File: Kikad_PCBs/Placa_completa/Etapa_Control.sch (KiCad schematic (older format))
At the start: 27 parts, among them U1 UC2844N, U2 PC817, U3 TL431

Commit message: modificaciones al pcb
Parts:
- C5: value 15n -> 1.5n
- RV1: value 5k -> 1k
- Rbledder1: value 22k -> 10K
- Rcs1: value 4k2 -> 3K9
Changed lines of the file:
@@
 P 4800 3450
 F 0 "Rcs1" V 4880 3450 39  0000 C CNN
-F 1 "4k2" V 4800 3450 39  0000 C CNN
+F 1 "3K9" V 4800 3450 39  0000 C CNN
 F 2 "Resistors_THT:R_Axial_DIN0207_L6.3mm_D2.5mm_P7.62mm_Horizontal" V 4730 3450 50  0001 C CNN
 F 3 "" H 4800 3450 50  0001 C CNN
@@
 P 6650 2600
 F 0 "Rbledder1" V 6730 2600 39  0000 C CNN
-F 1 "22k" V 6650 2600 39  0000 C CNN
+F 1 "10K" V 6650 2600 39  0000 C CNN
 F 2 "Resistors_THT:R_Axial_DIN0207_L6.3mm_D2.5mm_P7.62mm_Horizontal" V 6580 2600 50  0001 C CNN
 F 3 "" H 6650 2600 50  0001 C CNN
@@
 P 9600 4600
 F 0 "C5" H 9625 4700 50  0000 L CNN
-F 1 "15n" H 9625 4500 39  0000 L CNN
+F 1 "1.5n" H 9625 4500 39  0000 L CNN
 F 2 "Capacitors_THT:C_Disc_D5.0mm_W2.5mm_P2.50mm" H 9638 4450 50  0001 C CNN
 F 3 "" H 9600 4600 50  0001 C CNN
@@
 P 5850 5450
 F 0 "RV1" V 5675 5450 39  0000 C CNN
-F 1 "5k" V 5750 5450 39  0000 C CNN
+F 1 "1k" V 5750 5450 39  0000 C CNN
 F 2 "Potentiometers:Potentiometer_Trimmer_Bourns_3296W" H 5850 5450 50  0001 C CNN
 F 3 "" H 5850 5450 50  0001 C CNN

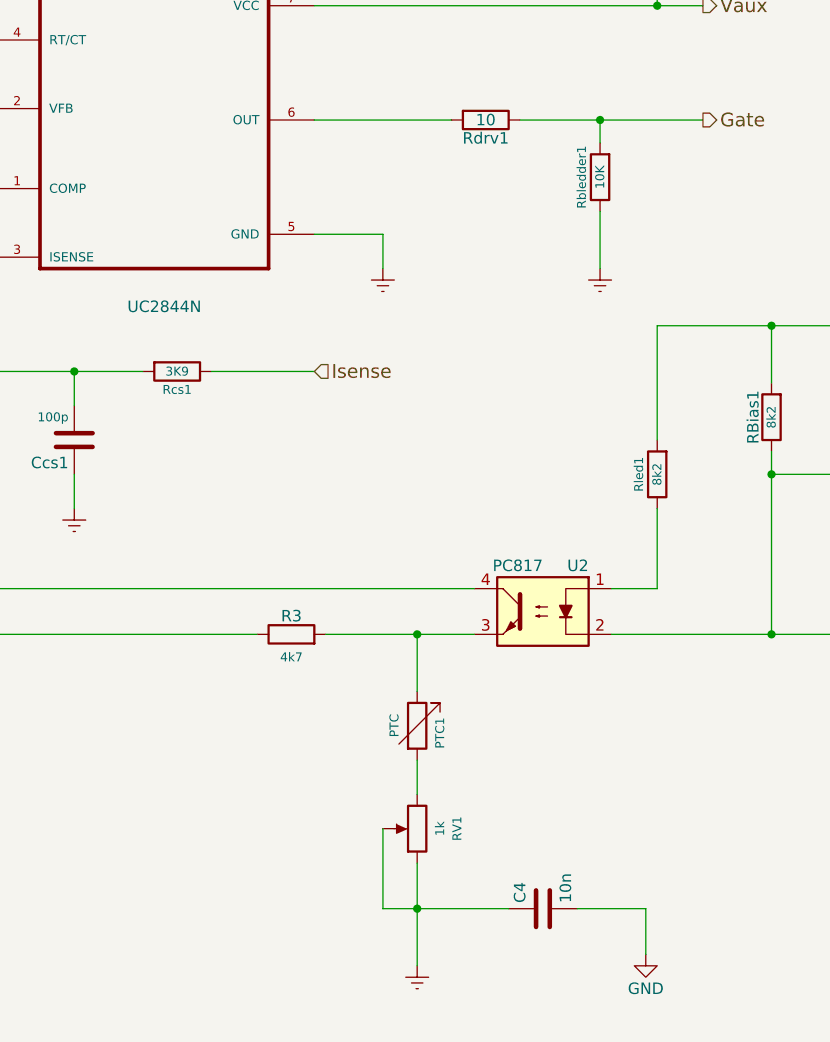
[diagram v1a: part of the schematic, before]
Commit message: cambio proyecto kicad por el que usamos en la primer fuente completa y modificacion de tamaños, bordes rellenos adaptado a la placa final. Falta ver que queden bien las serigrafias y modificar los componentes qe hizo el riojano para que queden todas las serigrafias bien
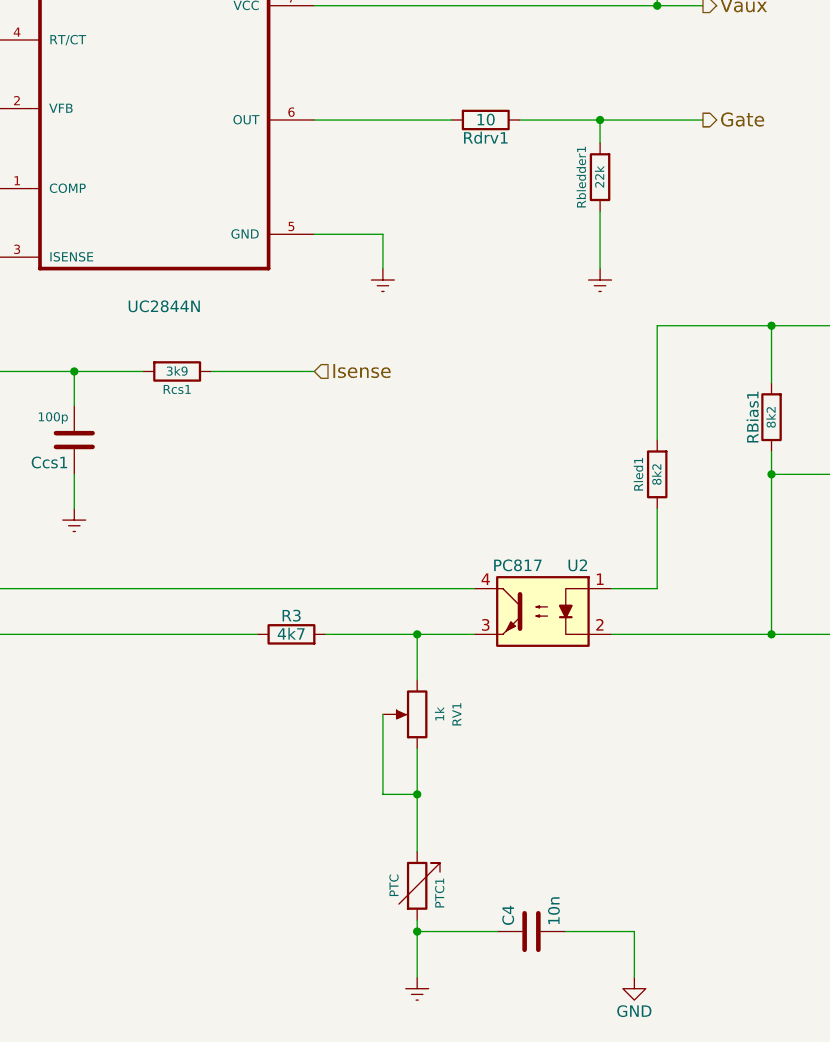
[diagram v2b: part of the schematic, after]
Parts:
- Rbledder1: value 10K -> 22k
- Rcs1: value 3K9 -> 3k9
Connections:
- net Earth: now also PTC1.2; no longer RV1.1, RV1.2
- net at R3.2, U2.3: now also RV1.3; no longer PTC1.1
- new net: PTC1.1, RV1.1, RV1.2
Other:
- moved on the sheet: C4, PTC1, RV1
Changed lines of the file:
@@
 P 4800 3450
 F 0 "Rcs1" V 4880 3450 39  0000 C CNN
-F 1 "3K9" V 4800 3450 39  0000 C CNN
+F 1 "3k9" V 4800 3450 39  0000 C CNN
 F 2 "Resistors_THT:R_Axial_DIN0207_L6.3mm_D2.5mm_P7.62mm_Horizontal" V 4730 3450 50  0001 C CNN
 F 3 "" H 4800 3450 50  0001 C CNN
@@
 P 5300 4600
 F 0 "R3" V 5380 4600 50  0000 C CNN
-F 1 "4k7" V 5200 4600 39  0000 C CNN
+F 1 "4k7" V 5300 4600 50  0000 C CNN
 F 2 "Resistors_THT:R_Axial_DIN0204_L3.6mm_D1.6mm_P7.62mm_Horizontal" V 5230 4600 50  0001 C CNN
 F 3 "" H 5300 4600 50  0001 C CNN
@@
 P 6650 2600
 F 0 "Rbledder1" V 6730 2600 39  0000 C CNN
-F 1 "10K" V 6650 2600 39  0000 C CNN
+F 1 "22k" V 6650 2600 39  0000 C CNN
 F 2 "Resistors_THT:R_Axial_DIN0207_L6.3mm_D2.5mm_P7.62mm_Horizontal" V 6580 2600 50  0001 C CNN
 F 3 "" H 6650 2600 50  0001 C CNN
@@
 L C C4
 U 1 1 5C1827A1
-P 6400 5800
-F 0 "C4" H 6425 5900 50  0000 L CNN
-F 1 "10n" H 6425 5700 50  0000 L CNN
-F 2 "Capacitors_THT:C_Rect_L4.0mm_W2.5mm_P2.50mm" H 6438 5650 50  0001 C CNN
-F 3 "" H 6400 5800 50  0001 C CNN
-	1    6400 5800
+P 6350 5900
+F 0 "C4" H 6375 6000 50  0000 L CNN
+F 1 "10n" H 6375 5800 50  0000 L CNN
+F 2 "Capacitors_THT:C_Rect_L4.0mm_W2.5mm_P2.50mm" H 6388 5750 50  0001 C CNN
+F 3 "" H 6350 5900 50  0001 C CNN
+	1    6350 5900
 	0    -1   -1   0
 $EndComp
@@
 	5450 4600 6100 4600
 Wire Wire Line
+	5850 4600 5850 4800
+Wire Wire Line
 	3300 4600 5150 4600
 Connection ~ 3300 2950
@@
 	8500 6100 8500 5750
 Wire Wire Line
-	6550 5800 6850 5800
-Wire Wire Line
-	5850 5600 5850 6050
+	6500 5900 6800 5900
+Wire Wire Line
+	5850 5100 5850 5550
 $Comp
 L GND #PWR024
 U 1 1 5C182AC4
-P 6850 6000
-F 0 "#PWR024" H 6850 5750 50  0001 C CNN
-F 1 "GND" H 6850 5850 50  0000 C CNN
-F 2 "" H 6850 6000 50  0001 C CNN
-F 3 "" H 6850 6000 50  0001 C CNN
-	1    6850 6000
+P 6800 6100
+F 0 "#PWR024" H 6800 5850 50  0001 C CNN
+F 1 "GND" H 6800 5950 50  0000 C CNN
+F 2 "" H 6800 6100 50  0001 C CNN
+F 3 "" H 6800 6100 50  0001 C CNN
+	1    6800 6100
 	1    0    0    -1
 $EndComp
@@
 L Earth #PWR027
 U 1 1 5C183232
-P 5850 6050
-F 0 "#PWR027" H 5850 5800 50  0001 C CNN
-F 1 "Earth" H 5850 5900 50  0001 C CNN
-F 2 "" H 5850 6050 50  0001 C CNN
-F 3 "" H 5850 6050 50  0001 C CNN
-	1    5850 6050
-	1    0    0    -1
-$EndComp
-Connection ~ 5850 5800
+P 5850 6100
+F 0 "#PWR027" H 5850 5850 50  0001 C CNN
+F 1 "Earth" H 5850 5950 50  0001 C CNN
+F 2 "" H 5850 6100 50  0001 C CNN
+F 3 "" H 5850 6100 50  0001 C CNN
+	1    5850 6100
+	1    0    0    -1
+$EndComp
+Connection ~ 5850 5300
 $Comp
 L Earth #PWR028
@@
 L POT RV1
 U 1 1 5C1AE9F6
-P 5850 5450
-F 0 "RV1" V 5675 5450 39  0000 C CNN
-F 1 "1k" V 5750 5450 39  0000 C CNN
-F 2 "Potentiometers:Potentiometer_Trimmer_Bourns_3296W" H 5850 5450 50  0001 C CNN
-F 3 "" H 5850 5450 50  0001 C CNN
-	1    5850 5450
-	-1   0    0    1
-$EndComp
-Wire Wire Line
-	5700 5450 5700 5800
+P 5850 4950
+F 0 "RV1" V 5675 4950 39  0000 C CNN
+F 1 "1k" V 5750 4950 39  0000 C CNN
+F 2 "Potentiometers:Potentiometer_Trimmer_Bourns_3296W" H 5850 4950 50  0001 C CNN
+F 3 "" H 5850 4950 50  0001 C CNN
+	1    5850 4950
+	-1   0    0    1
+$EndComp
+Wire Wire Line
+	5700 4950 5700 5300
 $Comp
 L R_Variable PTC1
 U 1 1 5C1AD7CF
-P 5850 5000
-F 0 "PTC1" V 5950 4900 39  0000 L CNN
-F 1 "PTC" V 5750 4950 39  0000 L CNN
-F 2 "Resistors_THT:R_Axial_DIN0207_L6.3mm_D2.5mm_P7.62mm_Horizontal" V 5780 5000 50  0001 C CNN
-F 3 "" H 5850 5000 50  0001 C CNN
-	1    5850 5000
-	1    0    0    -1
-$EndComp
-Wire Wire Line
-	6850 5800 6850 6000
-Wire Wire Line
-	5700 5800 6250 5800
-Wire Wire Line
-	5850 5300 5850 5150
-Wire Wire Line
-	5850 4850 5850 4600
+P 5850 5700
+F 0 "PTC1" V 5950 5600 39  0000 L CNN
+F 1 "PTC" V 5750 5650 39  0000 L CNN
+F 2 "Resistors_THT:R_Axial_DIN0207_L6.3mm_D2.5mm_P7.62mm_Horizontal" V 5780 5700 50  0001 C CNN
+F 3 "" H 5850 5700 50  0001 C CNN
+	1    5850 5700
+	1    0    0    -1
+$EndComp
+Wire Wire Line
+	6800 5900 6800 6100
+Wire Wire Line
+	5700 5300 5850 5300
+Wire Wire Line
+	5850 5850 5850 6100
+Wire Wire Line
+	6200 5900 5850 5900
+Connection ~ 5850 5900
 $EndSCHEMATC
